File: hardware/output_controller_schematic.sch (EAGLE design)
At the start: 27 parts, among them IC1 PIC16F1939-I_P, IC2 DAC102S085CIMM_NOPB, IC3 LM6211MF, IC4 LM6211MF, Q1 20MHz

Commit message: pwm outputs completed
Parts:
- added PWM1, PWM2, PWM3, PWM4: (no value), con-amp:MTA02-156
- added Q2, Q3, Q4: IRF1010NSPBF, IRF1010NSPBF:IRF1010NSPBF
- added R10, R12, R14, R8: 10k, rcl:R-EU_R1206
- added R11, R13, R15, R9: 100k, rcl:R-EU_R1206
- added Y1: 20MHz, adafruit:CRYSTALHC49S
- Q1: value 20MHz -> IRF1010NSPBF; device adafruit:CRYSTALHC49S -> IRF1010NSPBF:IRF1010NSPBF
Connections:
- new net N$10: PWM1.2, Q1.D
- new net N$11: Q2.G, R10.1, R11.2
- new net N$12: PWM2.2, Q2.D
- new net N$13: Q3.G, R12.1, R13.2
- new net N$14: PWM3.2, Q3.D
- new net N$15: Q4.G, R14.1, R15.2
- new net N$16: PWM4.2, Q4.D
- new net N$9: Q1.G, R8.1, R9.2
- net +24V: now also PWM1.1, PWM2.1, PWM3.1, PWM4.1
- net CLKIN: now also Y1.1; no longer Q1.1
- net CLKOUT: now also Y1.2; no longer Q1.2
- net GND: now also Q1.S, Q2.S, Q3.S, Q4.S, R11.1, R13.1, R15.1, R9.1
- net PWM1: now also R8.2
- net PWM2: now also R10.2
- net PWM3: now also R12.2
- net PWM4: now also R14.2
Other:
- moved on the sheet: ANOUT1, ANOUT2, C5, C6, C7, C8, IC2, IC3, IC4, R4, R5, R6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

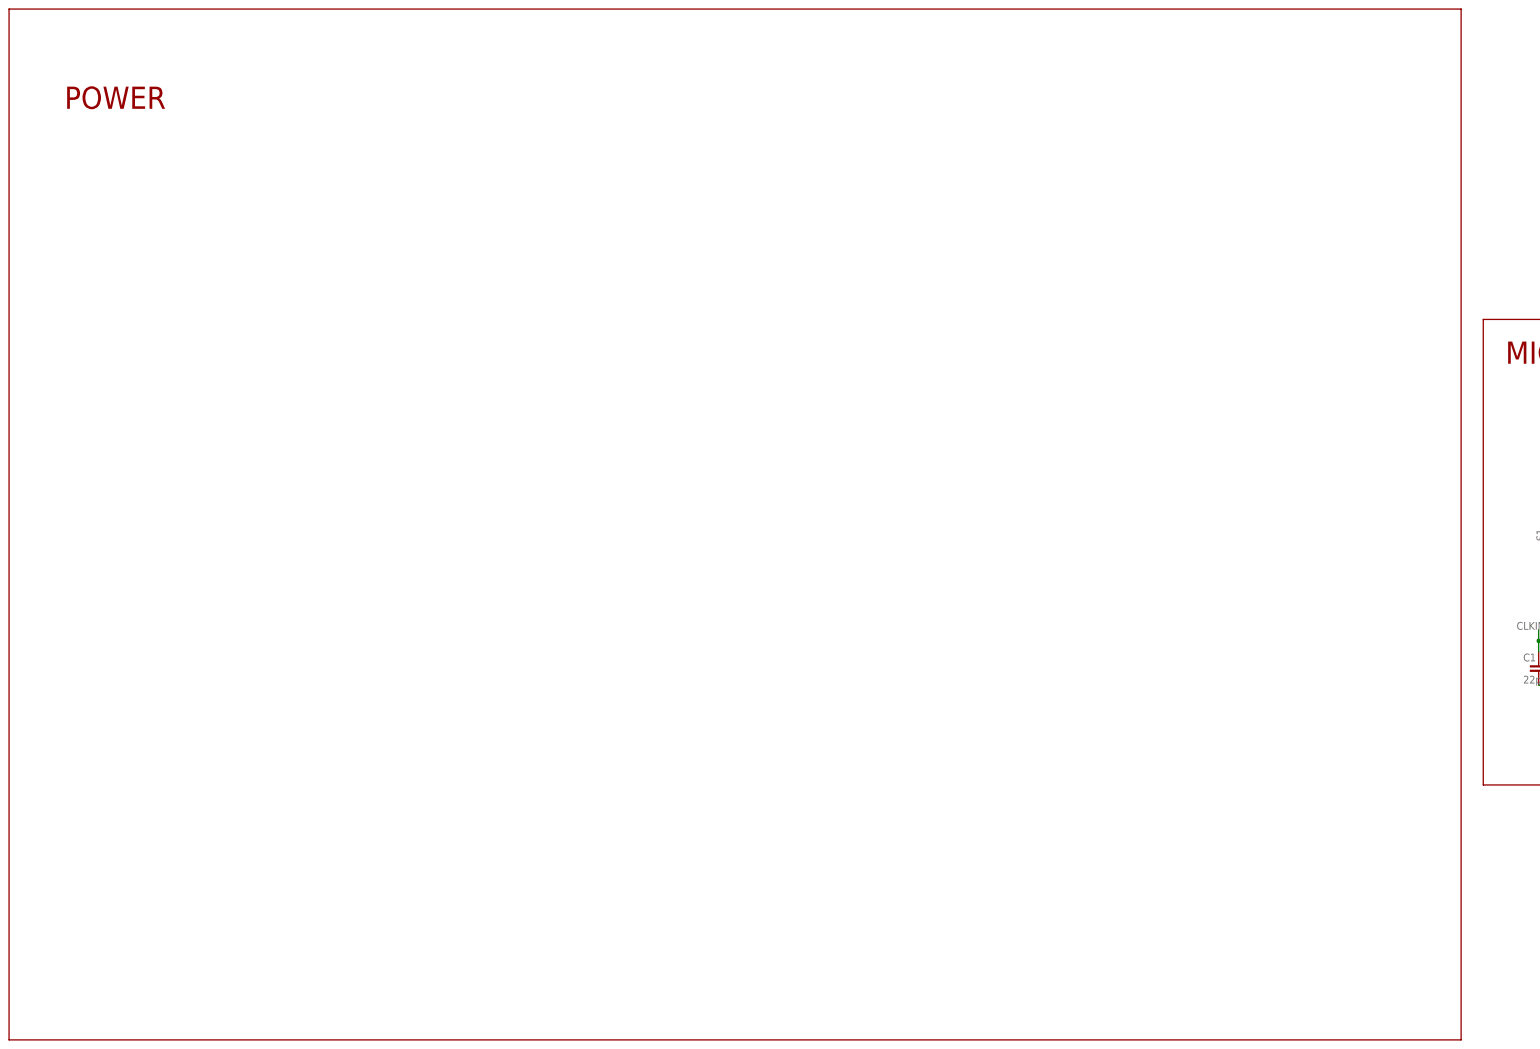
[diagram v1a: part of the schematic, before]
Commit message: complete schematic design and PCB layout generated
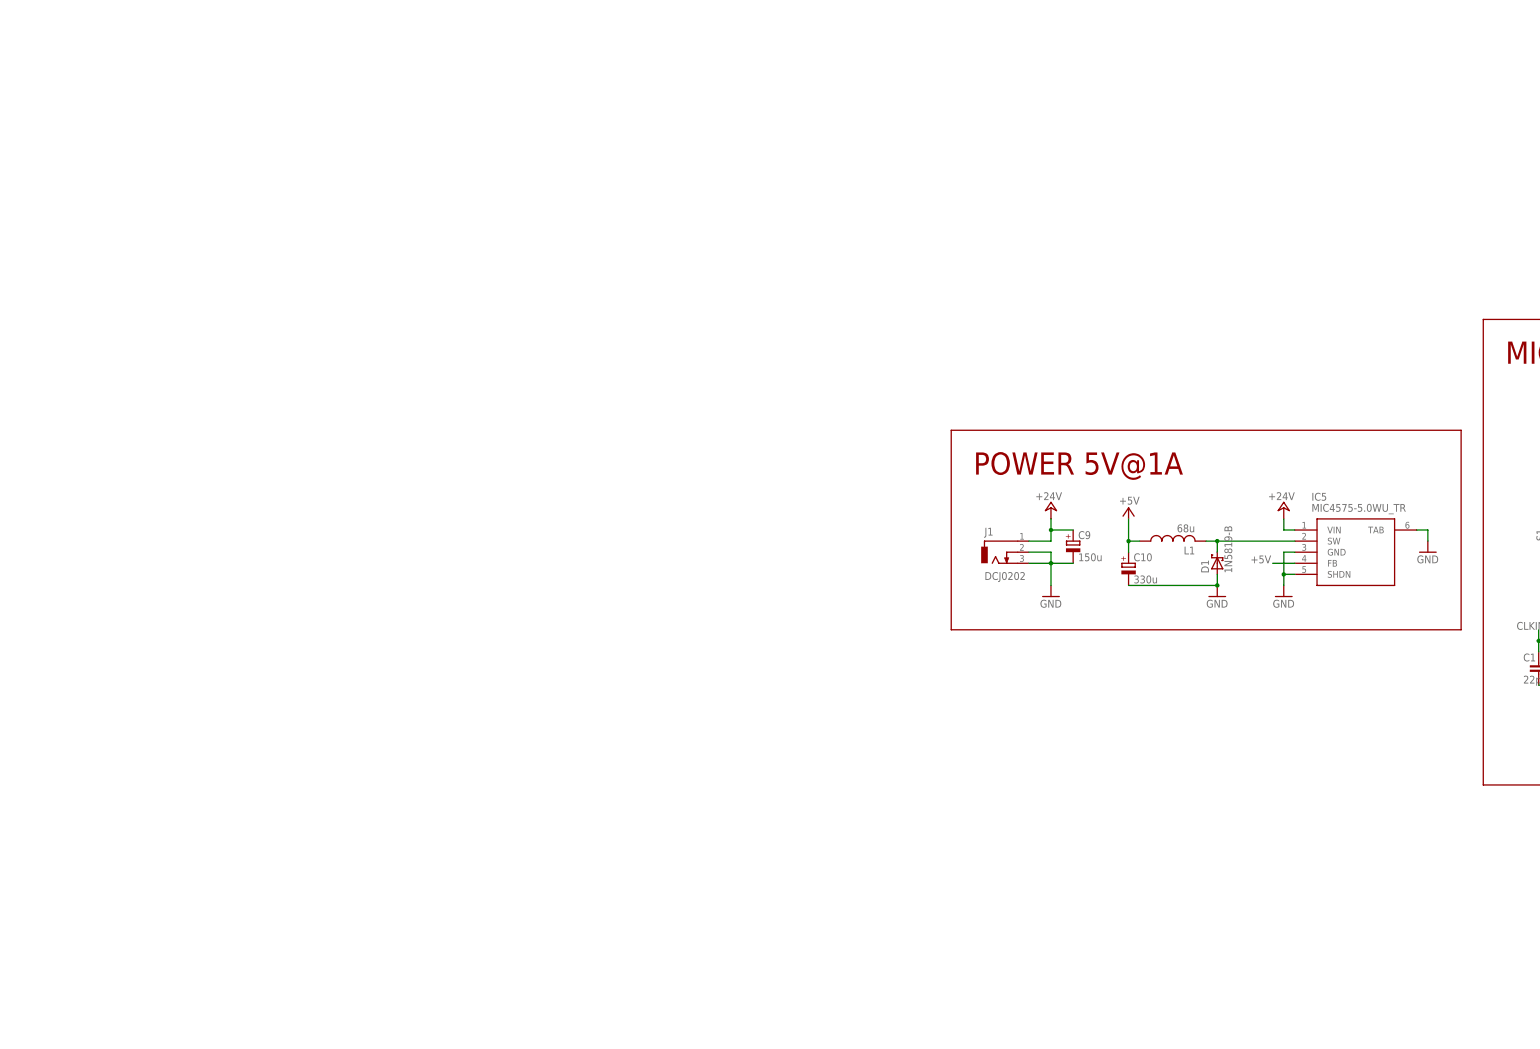
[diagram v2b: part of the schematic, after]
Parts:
- added C10: 330u, rcl:CPOL-EU175TMP-0810
- added C9: 150u, rcl:CPOL-EU175TMP-0810
- added D1: 1N5819-B, diode:1N5819-B
- added IC5: MIC4575-5.0WU_TR, MIC4575-5.0WU_TR:MIC4575-5.0WU_TR
- added J1: DCJ0202, con-jack:DCJ0202
- added L1: 68u, rcl:L-USL5650M
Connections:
- new net N$18: D1.C, IC5.SW, L1.2
- net +24V: now also C9.+, IC5.VIN, J1.1
- net +5V: now also C10.+, IC5.FB, L1.1
- net GND: now also C10.-, C9.-, D1.A, IC5.GND, IC5.SHDN, IC5.TAB, J1.2, J1.3
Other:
- note added: "POWER 5V@1A"
- note removed: "POWER"
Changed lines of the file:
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@@
 <part name="Q4" library="IRF1010NSPBF" deviceset="IRF1010NSPBF" device=""/>
 <part name="P+14" library="supply1" library_urn="urn:adsk.eagle:library:371" deviceset="+24V" device=""/>
+<part name="J1" library="con-jack" library_urn="urn:adsk.eagle:library:154" deviceset="DCJ0202" device="" package3d_urn="urn:adsk.eagle:package:7491/1"/>
+<part name="P+15" library="supply1" library_urn="urn:adsk.eagle:library:371" deviceset="+24V" device=""/>
+<part name="GND28" library="supply1" library_urn="urn:adsk.eagle:library:371" deviceset="GND" device=""/>
+<part name="IC5" library="MIC4575-5.0WU_TR" deviceset="MIC4575-5.0WU_TR" device=""/>
+<part name="C10" library="rcl" library_urn="urn:adsk.eagle:library:334" deviceset="CPOL-EU" device="175TMP-0810" package3d_urn="urn:adsk.eagle:package:23407/1" value="330u"/>
+<part name="C9" library="rcl" library_urn="urn:adsk.eagle:library:334" deviceset="CPOL-EU" device="175TMP-0810" package3d_urn="urn:adsk.eagle:package:23407/1" value="150u"/>
+<part name="GND29" library="supply1" library_urn="urn:adsk.eagle:library:371" deviceset="GND" device=""/>
+<part name="L1" library="rcl" library_urn="urn:adsk.eagle:library:334" deviceset="L-US" device="L5650M" package3d_urn="urn:adsk.eagle:package:23487/1" value="68u"/>
+<part name="GND30" library="supply1" library_urn="urn:adsk.eagle:library:371" deviceset="GND" device=""/>
+<part name="P+16" library="supply1" library_urn="urn:adsk.eagle:library:371" deviceset="+24V" device=""/>
+<part name="D1" library="diode" library_urn="urn:adsk.eagle:library:210" deviceset="1N581*" device="" package3d_urn="urn:adsk.eagle:package:43421/1" technology="9-B"/>
+<part name="GND31" library="supply1" library_urn="urn:adsk.eagle:library:371" deviceset="GND" device=""/>
+<part name="P+17" library="supply1" library_urn="urn:adsk.eagle:library:371" deviceset="+5V" device=""/>
 </parts>
 <sheets>
 <sheet>
 <plain>
-<wire x1="-426.72" y1="116.84" x2="-426.72" y2="-119.38" width="0.1524" layer="94"/>
-<wire x1="-426.72" y1="-119.38" x2="-93.98" y2="-119.38" width="0.1524" layer="94"/>
-<wire x1="-93.98" y1="-119.38" x2="-93.98" y2="116.84" width="0.1524" layer="94"/>
-<wire x1="-93.98" y1="116.84" x2="-426.72" y2="116.84" width="0.1524" layer="94"/>
-<text x="-414.02" y="93.98" size="5.08" layer="94">POWER</text>
+<wire x1="-210.82" y1="20.32" x2="-210.82" y2="-25.4" width="0.1524" layer="94"/>
+<wire x1="-210.82" y1="-25.4" x2="-93.98" y2="-25.4" width="0.1524" layer="94"/>
+<wire x1="-93.98" y1="-25.4" x2="-93.98" y2="20.32" width="0.1524" layer="94"/>
+<wire x1="-93.98" y1="20.32" x2="-210.82" y2="20.32" width="0.1524" layer="94"/>
+<text x="-205.74" y="10.16" size="5.08" layer="94">POWER 5V@1A</text>
 <wire x1="-88.9" y1="45.72" x2="-88.9" y2="-60.96" width="0.1524" layer="94"/>
 <wire x1="-88.9" y1="-60.96" x2="78.74" y2="-60.96" width="0.1524" layer="94"/>
@@
 <attribute name="VALUE" x="187.96" y="-59.944" size="1.778" layer="96" rot="R180"/>
 </instance>
+<instance part="J1" gate="G$1" x="-200.66" y="-7.62" smashed="yes">
+<attribute name="NAME" x="-203.2" y="-3.81" size="1.778" layer="95"/>
+<attribute name="VALUE" x="-203.2" y="-13.97" size="1.778" layer="96"/>
+</instance>
+<instance part="P+15" gate="1" x="-187.96" y="2.54" smashed="yes">
+<attribute name="VALUE" x="-185.42" y="6.096" size="1.778" layer="96" rot="R180"/>
+</instance>
+<instance part="GND28" gate="1" x="-187.96" y="-17.78" smashed="yes">
+<attribute name="VALUE" x="-190.5" y="-20.32" size="1.778" layer="96"/>
+</instance>
+<instance part="IC5" gate="G$1" x="-132.08" y="-2.54" smashed="yes">
+<attribute name="NAME" x="-128.27" y="5.08" size="1.778" layer="95" align="center-left"/>
+<attribute name="VALUE" x="-128.27" y="2.54" size="1.778" layer="96" align="center-left"/>
+</instance>
+<instance part="C10" gate="G$1" x="-170.18" y="-10.16" smashed="yes">
+<attribute name="NAME" x="-169.037" y="-9.6774" size="1.778" layer="95"/>
+<attribute name="VALUE" x="-169.037" y="-14.7574" size="1.778" layer="96"/>
+</instance>
+<instance part="C9" gate="G$1" x="-182.88" y="-5.08" smashed="yes">
+<attribute name="NAME" x="-181.737" y="-4.5974" size="1.778" layer="95"/>
+<attribute name="VALUE" x="-181.737" y="-9.6774" size="1.778" layer="96"/>
+</instance>
+<instance part="GND29" gate="1" x="-134.62" y="-17.78" smashed="yes">
+<attribute name="VALUE" x="-137.16" y="-20.32" size="1.778" layer="96"/>
+</instance>
+<instance part="L1" gate="G$1" x="-160.02" y="-5.08" smashed="yes" rot="R90">
+<attribute name="NAME" x="-154.94" y="-6.35" size="1.778" layer="95" rot="R180"/>
+<attribute name="VALUE" x="-154.94" y="-1.27" size="1.778" layer="96" rot="R180"/>
+</instance>
+<instance part="GND30" gate="1" x="-101.6" y="-7.62" smashed="yes">
+<attribute name="VALUE" x="-104.14" y="-10.16" size="1.778" layer="96"/>
+</instance>
+<instance part="P+16" gate="1" x="-134.62" y="2.54" smashed="yes">
+<attribute name="VALUE" x="-132.08" y="6.096" size="1.778" layer="96" rot="R180"/>
+</instance>
+<instance part="D1" gate="G$1" x="-149.86" y="-10.16" smashed="yes" rot="R90">
+<attribute name="NAME" x="-151.765" y="-12.446" size="1.778" layer="95" rot="R90"/>
+<attribute name="VALUE" x="-146.431" y="-12.446" size="1.778" layer="96" rot="R90"/>
+</instance>
+<instance part="GND31" gate="1" x="-149.86" y="-17.78" smashed="yes">
+<attribute name="VALUE" x="-152.4" y="-20.32" size="1.778" layer="96"/>
+</instance>
+<instance part="P+17" gate="1" x="-170.18" y="2.54" smashed="yes">
+<attribute name="VALUE" x="-167.64" y="5.08" size="1.778" layer="96" rot="R180"/>
+</instance>
 </instances>
 <busses>
@@
 <wire x1="185.42" y1="-99.06" x2="185.42" y2="-88.9" width="0.1524" layer="91"/>
 </segment>
+<segment>
+<pinref part="J1" gate="G$1" pin="3"/>
+<wire x1="-193.04" y1="-10.16" x2="-187.96" y2="-10.16" width="0.1524" layer="91"/>
+<pinref part="GND28" gate="1" pin="GND"/>
+<wire x1="-187.96" y1="-10.16" x2="-187.96" y2="-15.24" width="0.1524" layer="91"/>
+<pinref part="J1" gate="G$1" pin="2"/>
+<wire x1="-193.04" y1="-7.62" x2="-187.96" y2="-7.62" width="0.1524" layer="91"/>
+<wire x1="-187.96" y1="-7.62" x2="-187.96" y2="-10.16" width="0.1524" layer="91"/>
+<junction x="-187.96" y="-10.16"/>
+<pinref part="C9" gate="G$1" pin="-"/>
+<wire x1="-182.88" y1="-10.16" x2="-187.96" y2="-10.16" width="0.1524" layer="91"/>
+</segment>
+<segment>
+<pinref part="IC5" gate="G$1" pin="SHDN"/>
+<wire x1="-132.08" y1="-12.7" x2="-134.62" y2="-12.7" width="0.1524" layer="91"/>
+<pinref part="GND29" gate="1" pin="GND"/>
+<wire x1="-134.62" y1="-12.7" x2="-134.62" y2="-15.24" width="0.1524" layer="91"/>
+<pinref part="IC5" gate="G$1" pin="GND"/>
+<wire x1="-132.08" y1="-7.62" x2="-134.62" y2="-7.62" width="0.1524" layer="91"/>
+<wire x1="-134.62" y1="-7.62" x2="-134.62" y2="-12.7" width="0.1524" layer="91"/>
+<junction x="-134.62" y="-12.7"/>
+</segment>
+<segment>
+<pinref part="GND30" gate="1" pin="GND"/>
+<wire x1="-101.6" y1="-5.08" x2="-101.6" y2="-2.54" width="0.1524" layer="91"/>
+<pinref part="IC5" gate="G$1" pin="TAB"/>
+<wire x1="-101.6" y1="-2.54" x2="-104.14" y2="-2.54" width="0.1524" layer="91"/>
+</segment>
+<segment>
+<pinref part="C10" gate="G$1" pin="-"/>
+<pinref part="GND31" gate="1" pin="GND"/>
+<wire x1="-170.18" y1="-15.24" x2="-149.86" y2="-15.24" width="0.1524" layer="91"/>
+<pinref part="D1" gate="G$1" pin="A"/>
+<wire x1="-149.86" y1="-12.7" x2="-149.86" y2="-15.24" width="0.1524" layer="91"/>
+<junction x="-149.86" y="-15.24"/>
+</segment>
 </net>
 <net name="+5V" class="0">
@@
 <pinref part="C3" gate="G$1" pin="1"/>
 <pinref part="C4" gate="G$1" pin="1"/>
+</segment>
+<segment>
+<pinref part="C10" gate="G$1" pin="+"/>
+<wire x1="-170.18" y1="-7.62" x2="-170.18" y2="-5.08" width="0.1524" layer="91"/>
+<pinref part="L1" gate="G$1" pin="1"/>
+<wire x1="-170.18" y1="-5.08" x2="-167.64" y2="-5.08" width="0.1524" layer="91"/>
+<pinref part="P+17" gate="1" pin="+5V"/>
+<wire x1="-170.18" y1="-5.08" x2="-170.18" y2="0" width="0.1524" layer="91"/>
+<junction x="-170.18" y="-5.08"/>
+</segment>
+<segment>
+<pinref part="IC5" gate="G$1" pin="FB"/>
+<wire x1="-132.08" y1="-10.16" x2="-137.16" y2="-10.16" width="0.1524" layer="91"/>
+<label x="-142.24" y="-10.16" size="1.778" layer="95"/>
 </segment>
 </net>
@@
 <wire x1="185.42" y1="-68.58" x2="185.42" y2="-66.04" width="0.1524" layer="91"/>
 </segment>
+<segment>
+<pinref part="J1" gate="G$1" pin="1"/>
+<wire x1="-193.04" y1="-5.08" x2="-187.96" y2="-5.08" width="0.1524" layer="91"/>
+<pinref part="P+15" gate="1" pin="+24V"/>
+<wire x1="-187.96" y1="-5.08" x2="-187.96" y2="-2.54" width="0.1524" layer="91"/>
+<pinref part="C9" gate="G$1" pin="+"/>
+<wire x1="-187.96" y1="-2.54" x2="-187.96" y2="0" width="0.1524" layer="91"/>
+<wire x1="-182.88" y1="-2.54" x2="-187.96" y2="-2.54" width="0.1524" layer="91"/>
+<junction x="-187.96" y="-2.54"/>
+</segment>
+<segment>
+<pinref part="IC5" gate="G$1" pin="VIN"/>
+<wire x1="-132.08" y1="-2.54" x2="-134.62" y2="-2.54" width="0.1524" layer="91"/>
+<pinref part="P+16" gate="1" pin="+24V"/>
+<wire x1="-134.62" y1="-2.54" x2="-134.62" y2="0" width="0.1524" layer="91"/>
+</segment>
 </net>
 <net name="N$4" class="0">
@@
 </segment>
 </net>
+<net name="N$18" class="0">
+<segment>
+<pinref part="L1" gate="G$1" pin="2"/>
+<pinref part="IC5" gate="G$1" pin="SW"/>
+<wire x1="-152.4" y1="-5.08" x2="-149.86" y2="-5.08" width="0.1524" layer="91"/>
+<pinref part="D1" gate="G$1" pin="C"/>
+<wire x1="-149.86" y1="-5.08" x2="-132.08" y2="-5.08" width="0.1524" layer="91"/>
+<wire x1="-149.86" y1="-7.62" x2="-149.86" y2="-5.08" width="0.1524" layer="91"/>
+<junction x="-149.86" y="-5.08"/>
+</segment>
+</net>

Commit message: first uncomplete organization of PCB layout
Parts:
- ANOUT1, ANOUT2: value (none) -> 22-23-2021; device con-amp:MTA02-156 -> con-molex:22-23-2021
- ICSP: device con-amp:MTA05-100 -> con-lstb:MA05-1
- UART: device con-amp:MTA04-100 -> con-lstb:MA04-1
- renumbered J1 to POWER
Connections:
- removed net N$1: IC1.RD3
- removed net N$2: IC1.RD2
- removed net PWM5: IC1.RE2
- net AN1: now also ANOUT1-1.S; no longer ANOUT1.1
- net AN2: now also ANOUT2-1.S; no longer ANOUT2.1
- net GND: now also ANOUT1-2.S, ANOUT2-2.S; no longer ANOUT1.2, ANOUT2.2

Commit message: start code and simulation with blinking leds
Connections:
- net CS: now also IC1.RD3; no longer IC1.RC0
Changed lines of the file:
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@@
 <net name="CS" class="0">
-<segment>
-<pinref part="IC1" gate="G$1" pin="RC0"/>
-<wire x1="-30.48" y1="-10.16" x2="-33.02" y2="-10.16" width="0.1524" layer="91"/>
-<label x="-38.1" y="-10.16" size="1.778" layer="95"/>
-</segment>
 <segment>
 <pinref part="IC2" gate="G$1" pin="!SYNC"/>
@@
 <label x="137.16" y="68.58" size="1.778" layer="95"/>
 </segment>
+<segment>
+<pinref part="IC1" gate="G$1" pin="RD3"/>
+<wire x1="27.94" y1="-20.32" x2="30.48" y2="-20.32" width="0.1524" layer="91"/>
+<label x="30.48" y="-20.32" size="1.778" layer="95"/>
+</segment>
 </net>
